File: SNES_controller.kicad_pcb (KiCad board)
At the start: 2 copper layers, 144 x 62 mm, 19 parts, among them J1 Conn_01x07, SW1 R, SW10 SELECT, SW11 Y, SW12 B, SW2 L, SW3 X, SW4 A, SW5 RIGHT, SW6 LEFT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

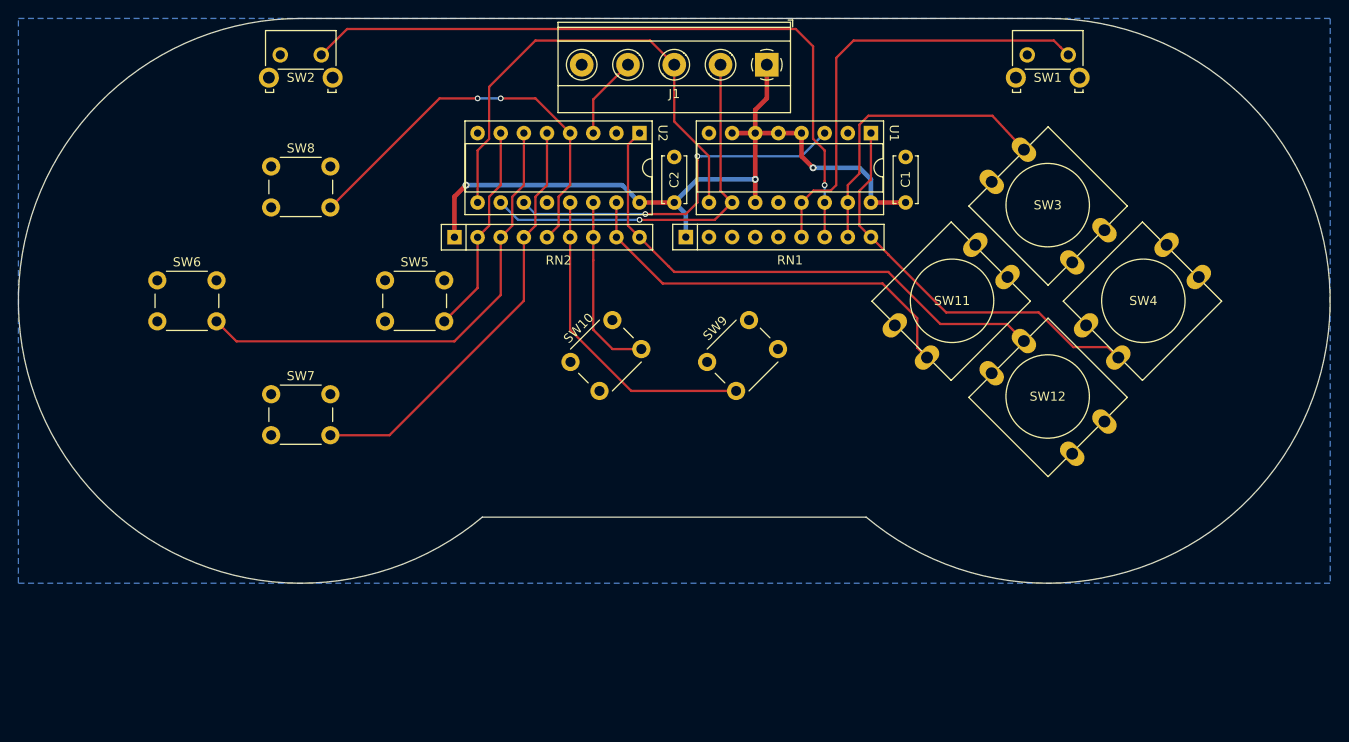
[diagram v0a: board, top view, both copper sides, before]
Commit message: Change switches to connectors, add logic to prevent UP/DOWN or LEFT/RIGHT from being pressed simultaneously.
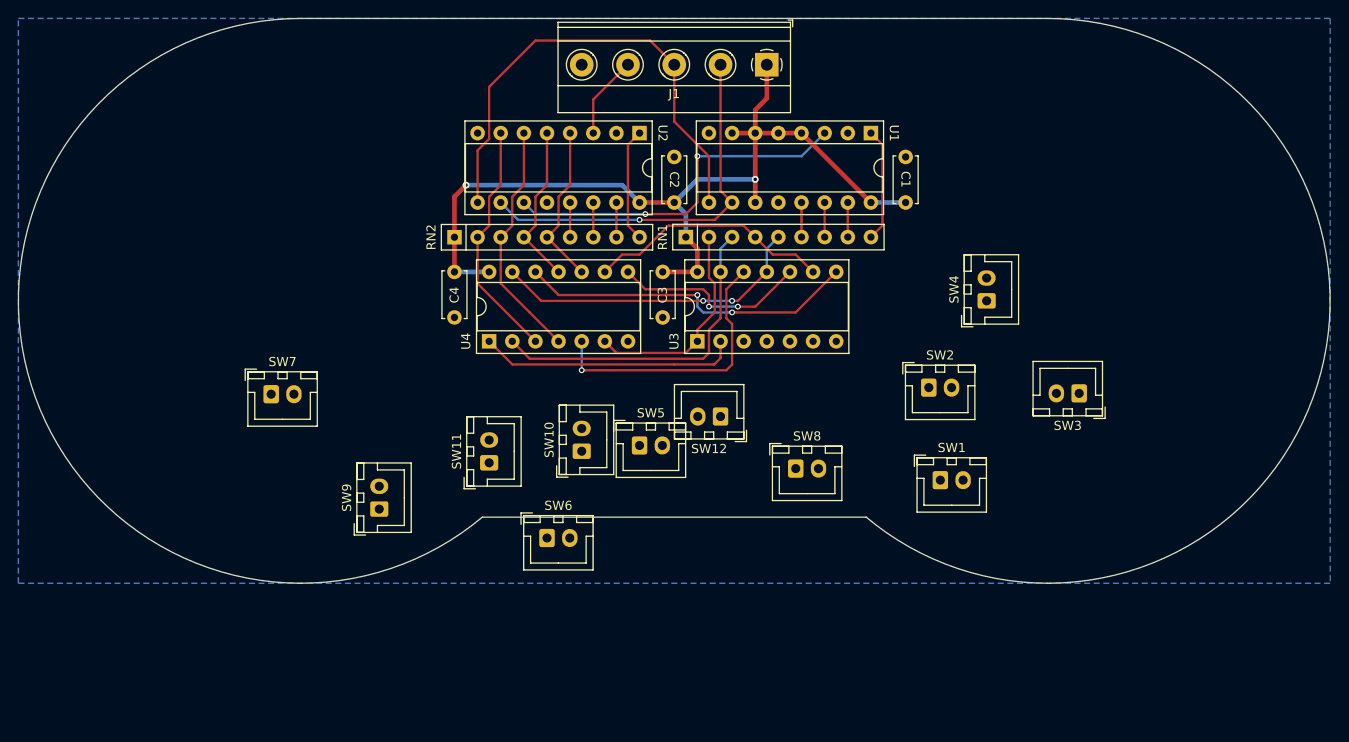
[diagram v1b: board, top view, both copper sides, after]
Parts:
- added C3: 100n, Capacitor_THT:C_Disc_D5.0mm_W2.5mm_P5.00mm, F.Cu at (-1.27, -3.17)
- added C4: 100n, Capacitor_THT:C_Disc_D5.0mm_W2.5mm_P5.00mm, F.Cu at (-24.1, -3.17)
- added U3: 4069, Package_DIP:DIP-14_W7.62mm_Socket, F.Cu at (2.54, 4.45)
- added U4: 4011, Package_DIP:DIP-14_W7.62mm_Socket, F.Cu at (-20.3, 4.45)
- SW1, SW2: footprint Button_Switch_THT:SW_Tactile_SKHH_Angled -> Connector_JST:JST_XH_B2B-XH-A_1x02_P2.50mm_Vertical
- SW10, SW5, SW6, SW7, SW8, SW9: footprint Button_Switch_THT:SW_PUSH_6mm_H8mm -> Connector_JST:JST_XH_B2B-XH-A_1x02_P2.50mm_Vertical
- SW11, SW12, SW3, SW4: footprint Button_Switch_THT:SW_PUSH-12mm -> Connector_JST:JST_XH_B2B-XH-A_1x02_P2.50mm_Vertical
- moved SW2 80.0 mm to (27.9, 9.53)
- moved SW8 66.5 mm to (13.3, 18.4)
- moved SW6 51.3 mm to (-14.0, 26.0)
- moved SW1 47.6 mm to (29.2, 19.7)
- moved SW11 47.0 mm to (-20.3, 17.8), turned to 90 degrees
- moved SW9 39.5 mm to (-32.4, 22.9), turned to 90 degrees
- moved SW12 38.8 mm to (5.08, 12.7), turned to 180 degrees
- moved SW5 33.3 mm to (-3.81, 15.9)
- moved SW3 14.4 mm to (44.5, 10.2), turned to 180 degrees
- moved SW4 11.2 mm to (34.3, 0.00), turned to 90 degrees
- moved SW10 9.88 mm to (-10.2, 16.5), turned to 90 degrees
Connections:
- RN2 pad 2: Net-(RN2-Pad2) -> /RIGHT
- RN2 pad 3: Net-(RN2-Pad3) -> /LEFT
- RN2 pad 4: Net-(RN2-Pad4) -> /DOWN
- RN2 pad 5: Net-(RN2-Pad5) -> /UP
- SW5 pad 2: Net-(RN2-Pad2) -> Net-(RN1-Pad2)
- SW6 pad 2: Net-(RN2-Pad3) -> Net-(RN1-Pad3)
- SW7 pad 2: Net-(RN2-Pad4) -> Net-(RN1-Pad4)
- SW8 pad 2: Net-(RN2-Pad5) -> Net-(RN1-Pad5)
- U2 pad 4: Net-(RN2-Pad5) -> /UP
- U2 pad 5: Net-(RN2-Pad4) -> /DOWN
- U2 pad 6: Net-(RN2-Pad3) -> /LEFT
- U2 pad 7: Net-(RN2-Pad2) -> /RIGHT
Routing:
- net Net-(RN1-Pad7): track 77.4 -> 3.81 mm, vias 1 -> 0
- net Net-(RN2-Pad3): track 53.0 -> 0.00 mm
- net Net-(RN2-Pad9): track 59.4 -> 12.5 mm
- net Net-(RN2-Pad4): track 46.8 -> 0.00 mm
- net Net-(RN1-Pad6): track 49.3 -> 3.81 mm
- net Net-(RN2-Pad5): track 45.3 -> 0.00 mm, vias 2 -> 0
- net Net-(RN2-Pad8): track 45.3 -> 3.81 mm
- net Net-(U3-Pad8): track 0.00 -> 37.4 mm, vias 0 -> 2
- net Net-(RN1-Pad3): track 0.00 -> 36.4 mm
- net Net-(RN1-Pad5): track 0.00 -> 34.9 mm, vias 0 -> 2
- net Net-(RN1-Pad9): track 45.1 -> 12.5 mm
- net Net-(RN2-Pad6): track 35.0 -> 3.81 mm
- net Net-(U3-Pad12): track 0.00 -> 31.2 mm, vias 0 -> 1
- net Net-(RN1-Pad8): track 33.0 -> 3.81 mm
- net Net-(U3-Pad2): track 0.00 -> 28.6 mm
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
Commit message: Reroute PCB with new logic and connectors in place of switches.
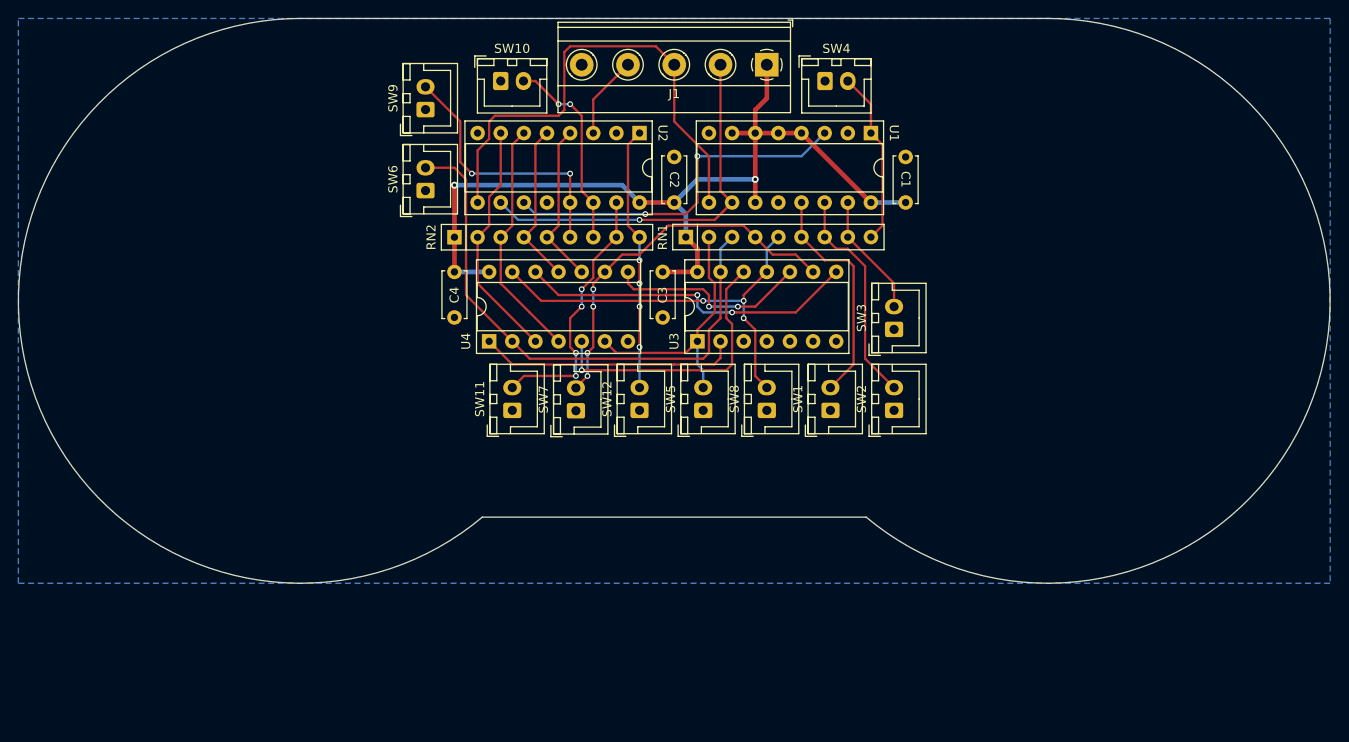
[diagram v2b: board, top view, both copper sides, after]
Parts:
- moved SW9 44.1 mm to (-27.3, -21.0)
- moved SW10 41.6 mm to (-19.1, -24.1), turned to 0 degrees
- moved SW6 40.4 mm to (-27.3, -12.1), turned to 90 degrees
- moved SW7 33.5 mm to (-10.8, 12.1), turned to 90 degrees
- moved SW4 29.9 mm to (16.6, -24.1), turned to 0 degrees
- moved SW3 21.5 mm to (24.1, 3.13), turned to 90 degrees
- moved SW1 14.3 mm to (17.1, 12.0), turned to 90 degrees
- moved SW12 8.92 mm to (-3.81, 12.0), turned to 90 degrees
- moved SW5 7.98 mm to (3.17, 12.0), turned to 90 degrees
- moved SW8 7.14 mm to (10.2, 12.0), turned to 90 degrees
- moved SW11 6.29 mm to (-17.8, 12.0)
- moved SW2 4.56 mm to (24.1, 12.0), turned to 90 degrees
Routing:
- net Net-(RN2-Pad6): track 3.81 -> 29.4 mm, vias 0 -> 2
- net Net-(RN2-Pad8): track 3.81 -> 28.9 mm, vias 0 -> 4
- net Net-(RN1-Pad3): track 36.4 -> 61.3 mm
- net Net-(RN1-Pad6): track 3.81 -> 26.1 mm
- net Net-(RN1-Pad7): track 3.81 -> 24.2 mm
- net Net-(RN2-Pad7): track 3.81 -> 21.8 mm, vias 0 -> 2
- net Net-(RN2-Pad9): track 12.5 -> 29.0 mm, vias 0 -> 4
- net Net-(RN1-Pad4): track 27.1 -> 41.2 mm, vias 0 -> 4
- net Net-(RN1-Pad5): track 34.9 -> 45.9 mm, vias 2 -> 3
- net Net-(RN1-Pad8): track 3.81 -> 13.5 mm
- net Net-(RN1-Pad9): track 12.5 -> 19.2 mm
- net Net-(RN1-Pad2): track 23.7 -> 29.1 mm
- net /SNES_LAT: track 53.5 -> 54.4 mm
- net Net-(U3-Pad10): track 21.7 -> 22.4 mm
- net +5V: track 97.8 -> 98.5 mm

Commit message: Finish redesign
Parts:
- moved C1 43.6 mm to (55.9, 20.3)
- moved U3 43.6 mm to (33.0, 35.6)
- moved C2 43.6 mm to (30.5, 20.3)
- moved C3 43.6 mm to (29.2, 27.9)
- moved C4 43.6 mm to (6.35, 27.9)
- moved J1 43.6 mm to (40.6, 5.20)
- moved RN1 43.6 mm to (31.8, 24.1)
- moved SW10 43.6 mm to (11.4, 6.99)
- moved SW4 43.6 mm to (47.0, 6.99)
- moved SW6 43.6 mm to (3.17, 19.0)
- moved SW9 43.6 mm to (3.17, 10.1)
- moved U1 43.6 mm to (52.1, 12.7)
- moved U2 43.6 mm to (26.7, 12.7)
- moved U4 43.6 mm to (10.2, 35.6)
- moved RN2 43.6 mm to (6.35, 24.1)
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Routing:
- net Net-(RN2-Pad8): track 28.9 -> 37.7 mm, vias 4 -> 6
- net Net-(RN2-Pad9): track 29.0 -> 36.4 mm, vias 4 -> 5
- net Net-(RN1-Pad4): track 41.2 -> 46.8 mm, vias 4 -> 3
- net /LEFT: track 26.5 -> 28.8 mm
- net Net-(RN1-Pad2): track 29.1 -> 27.5 mm, vias 0 -> 1
- net Net-(U3-Pad12): track 31.2 -> 30.4 mm
- net Net-(RN1-Pad7): track 24.2 -> 23.7 mm
- net Net-(RN1-Pad8): track 13.5 -> 13.0 mm
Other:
- board size 144 x 62 mm -> 57.8 x 46.4 mm

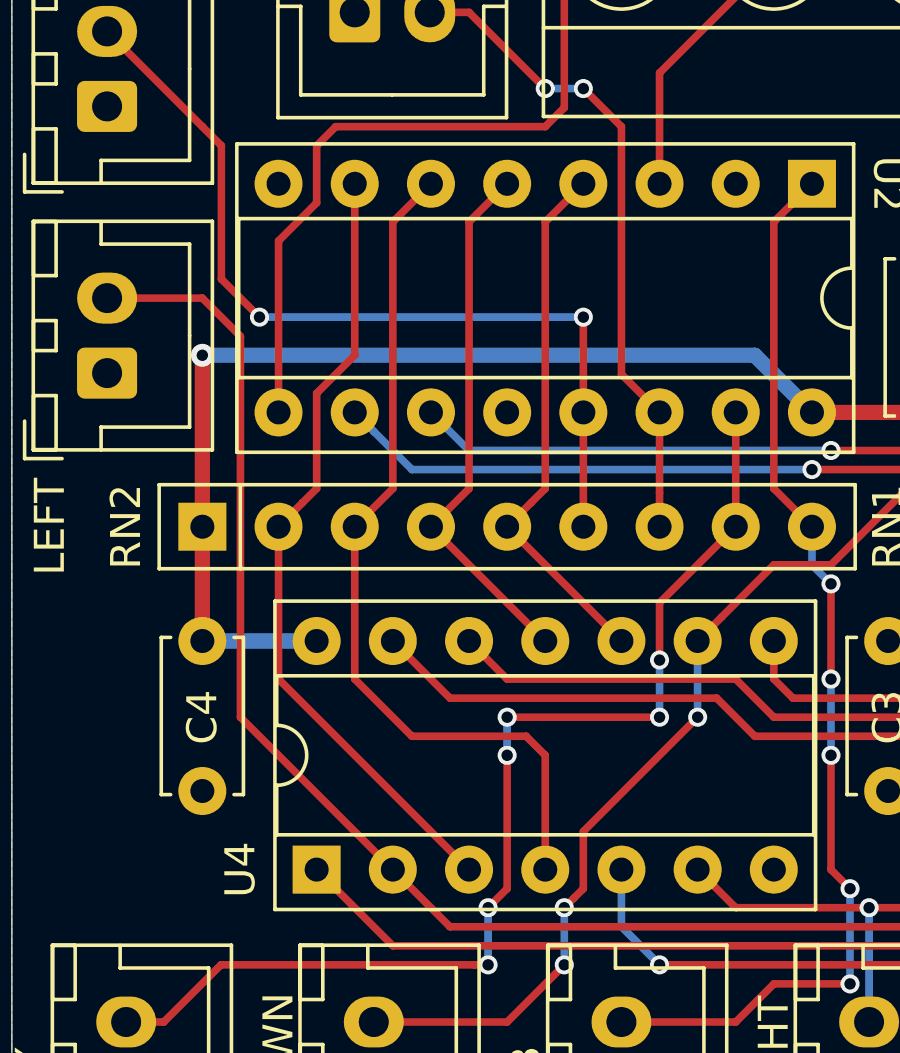
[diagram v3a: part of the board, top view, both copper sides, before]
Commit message: Disconnect unnecessary pullups
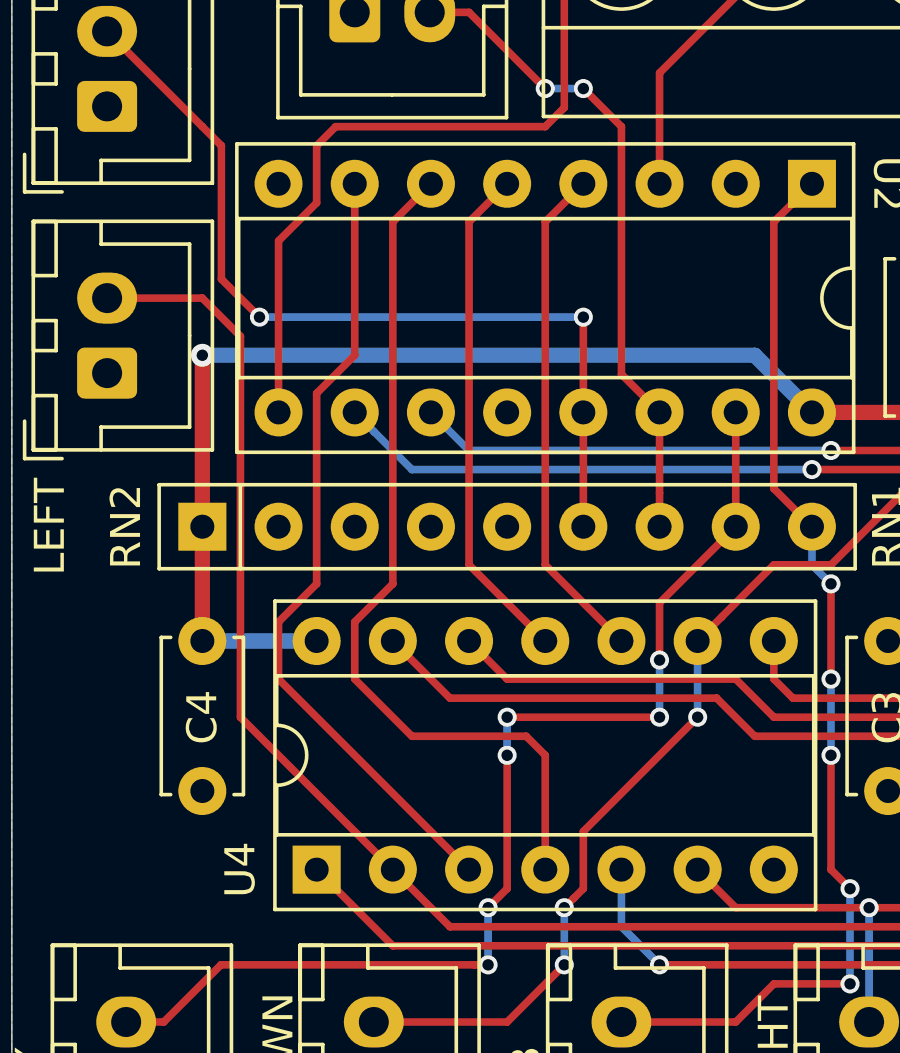
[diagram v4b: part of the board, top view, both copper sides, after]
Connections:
- RN2 pad 2: /RIGHT -> Net-(RN2-Pad2)
- RN2 pad 3: /LEFT -> Net-(RN2-Pad3)
- RN2 pad 4: /DOWN -> Net-(RN2-Pad4)
- RN2 pad 5: /UP -> Net-(RN2-Pad5)
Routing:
- net /UP: track 17.9 -> 16.8 mm
- net /DOWN: track 17.9 -> 16.8 mm
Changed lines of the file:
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@@
     (thickness 1.6)
     (drawings 6)
-    (tracks 259)
+    (tracks 255)
     (zones 0)
     (modules 23)
-    (nets 33)
+    (nets 37)
   )
   (page A4)
@@
   (net 31 "Net-(U3-Pad2)")
   (net 32 "Net-(U3-Pad8)")
+  (net 33 "Net-(RN2-Pad5)")
+  (net 34 "Net-(RN2-Pad4)")
+  (net 35 "Net-(RN2-Pad3)")
+  (net 36 "Net-(RN2-Pad2)")
   (net_class Default "This is the default net class."
     (clearance 0.1524)
@@
     (add_net "Net-(RN1-Pad8)")
     (add_net "Net-(RN1-Pad9)")
+    (add_net "Net-(RN2-Pad2)")
+    (add_net "Net-(RN2-Pad3)")
+    (add_net "Net-(RN2-Pad4)")
+    (add_net "Net-(RN2-Pad5)")
     (add_net "Net-(RN2-Pad6)")
     (add_net "Net-(RN2-Pad7)")
@@
       (net 17 "Net-(RN2-Pad6)"))
     (pad 5 thru_hole oval (at 10.16 0) (size 1.6 1.6) (drill 0.8) (layers *.Cu *.Mask)
-      (net 23 /UP))
+      (net 33 "Net-(RN2-Pad5)"))
     (pad 4 thru_hole oval (at 7.62 0) (size 1.6 1.6) (drill 0.8) (layers *.Cu *.Mask)
-      (net 24 /DOWN))
+      (net 34 "Net-(RN2-Pad4)"))
     (pad 3 thru_hole oval (at 5.08 0) (size 1.6 1.6) (drill 0.8) (layers *.Cu *.Mask)
-      (net 25 /LEFT))
+      (net 35 "Net-(RN2-Pad3)"))
     (pad 2 thru_hole oval (at 2.54 0) (size 1.6 1.6) (drill 0.8) (layers *.Cu *.Mask)
-      (net 26 /RIGHT))
+      (net 36 "Net-(RN2-Pad2)"))
     (pad 1 thru_hole rect (at 0 0) (size 1.6 1.6) (drill 0.8) (layers *.Cu *.Mask)
       (net 2 +5V))
@@
   (segment (start 33.469012 15.24) (end 33.02 15.24) (width 0.254) (layer B.Cu) (net 19))
   (via (at 27.305 21.59) (size 0.635) (drill 0.381) (layers F.Cu B.Cu) (net 19))
-  (segment (start 20.32 27.94) (end 16.51 24.13) (width 0.254) (layer F.Cu) (net 23))
-  (segment (start 17.78 13.97) (end 17.78 22.86) (width 0.254) (layer F.Cu) (net 23))
-  (segment (start 17.78 22.86) (end 17.309999 23.330001) (width 0.254) (layer F.Cu) (net 23))
+  (segment (start 17.78 25.4) (end 20.32 27.94) (width 0.254) (layer F.Cu) (net 23))
   (segment (start 19.05 12.7) (end 17.78 13.97) (width 0.254) (layer F.Cu) (net 23))
-  (segment (start 17.309999 23.330001) (end 16.51 24.13) (width 0.254) (layer F.Cu) (net 23))
-  (segment (start 17.78 27.94) (end 13.97 24.13) (width 0.254) (layer F.Cu) (net 24))
+  (segment (start 17.78 13.97) (end 17.78 25.4) (width 0.254) (layer F.Cu) (net 23))
+  (segment (start 15.24 25.4) (end 17.78 27.94) (width 0.254) (layer F.Cu) (net 24))
   (segment (start 16.51 12.7) (end 15.24 13.97) (width 0.254) (layer F.Cu) (net 24))
-  (segment (start 15.24 22.86) (end 13.97 24.13) (width 0.254) (layer F.Cu) (net 24))
-  (segment (start 15.24 13.97) (end 15.24 22.86) (width 0.254) (layer F.Cu) (net 24))
-  (segment (start 12.7 22.86) (end 11.43 24.13) (width 0.254) (layer F.Cu) (net 25))
-  (segment (start 13.97 12.7) (end 12.7 13.97) (width 0.254) (layer F.Cu) (net 25))
-  (segment (start 12.7 13.97) (end 12.7 22.86) (width 0.254) (layer F.Cu) (net 25))
-  (segment (start 11.43 24.13) (end 11.43 29.21) (width 0.254) (layer F.Cu) (net 25))
-  (segment (start 13.335 31.115) (end 17.145 31.115) (width 0.254) (layer F.Cu) (net 25))
-  (segment (start 11.43 29.21) (end 13.335 31.115) (width 0.254) (layer F.Cu) (net 25))
-  (segment (start 17.78 31.75) (end 17.78 35.56) (width 0.254) (layer F.Cu) (net 25))
-  (segment (start 17.145 31.115) (end 17.78 31.75) (width 0.254) (layer F.Cu) (net 25))
-  (segment (start 9.689999 23.330001) (end 8.89 24.13) (width 0.254) (layer F.Cu) (net 26))
-  (segment (start 10.16 22.86) (end 9.689999 23.330001) (width 0.254) (layer F.Cu) (net 26))
-  (segment (start 10.16 19.685) (end 10.16 22.86) (width 0.254) (layer F.Cu) (net 26))
+  (segment (start 15.24 13.97) (end 15.24 25.4) (width 0.254) (layer F.Cu) (net 24))
+  (segment (start 12.7 13.97) (end 13.97 12.7) (width 0.254) (layer F.Cu) (net 25))
+  (segment (start 12.7 26.035) (end 12.7 13.97) (width 0.254) (layer F.Cu) (net 25))
+  (segment (start 17.145 31.115) (end 13.335 31.115) (width 0.254) (layer F.Cu) (net 25))
+  (segment (start 17.78 31.75) (end 17.145 31.115) (width 0.254) (layer F.Cu) (net 25))
+  (segment (start 17.78 35.56) (end 17.78 31.75) (width 0.254) (layer F.Cu) (net 25))
+  (segment (start 11.43 27.305) (end 12.7 26.035) (width 0.254) (layer F.Cu) (net 25))
+  (segment (start 13.335 31.115) (end 11.43 29.21) (width 0.254) (layer F.Cu) (net 25))
+  (segment (start 11.43 29.21) (end 11.43 27.305) (width 0.254) (layer F.Cu) (net 25))
+  (segment (start 8.89 29.21) (end 15.24 35.56) (width 0.254) (layer F.Cu) (net 26))
+  (segment (start 11.43 18.415) (end 10.16 19.685) (width 0.254) (layer F.Cu) (net 26))
+  (segment (start 10.16 19.685) (end 10.16 26.035) (width 0.254) (layer F.Cu) (net 26))
+  (segment (start 10.16 26.035) (end 8.89 27.305) (width 0.254) (layer F.Cu) (net 26))
   (segment (start 11.43 12.7) (end 11.43 18.415) (width 0.254) (layer F.Cu) (net 26))
-  (segment (start 11.43 18.415) (end 10.16 19.685) (width 0.254) (layer F.Cu) (net 26))
-  (segment (start 8.89 29.21) (end 8.89 24.13) (width 0.254) (layer F.Cu) (net 26))
-  (segment (start 15.24 35.56) (end 8.89 29.21) (width 0.254) (layer F.Cu) (net 26))
+  (segment (start 8.89 27.305) (end 8.89 29.21) (width 0.254) (layer F.Cu) (net 26))
   (segment (start 36.83 38.1) (end 36.195 38.735) (width 0.254) (layer F.Cu) (net 28))
   (segment (start 36.83 33.655) (end 36.83 38.1) (width 0.254) (layer F.Cu) (net 28))
